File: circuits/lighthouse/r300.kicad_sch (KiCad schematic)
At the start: 18 parts, among them Q3 2N7002K, U1 R300, U6 AMS1117-3.3

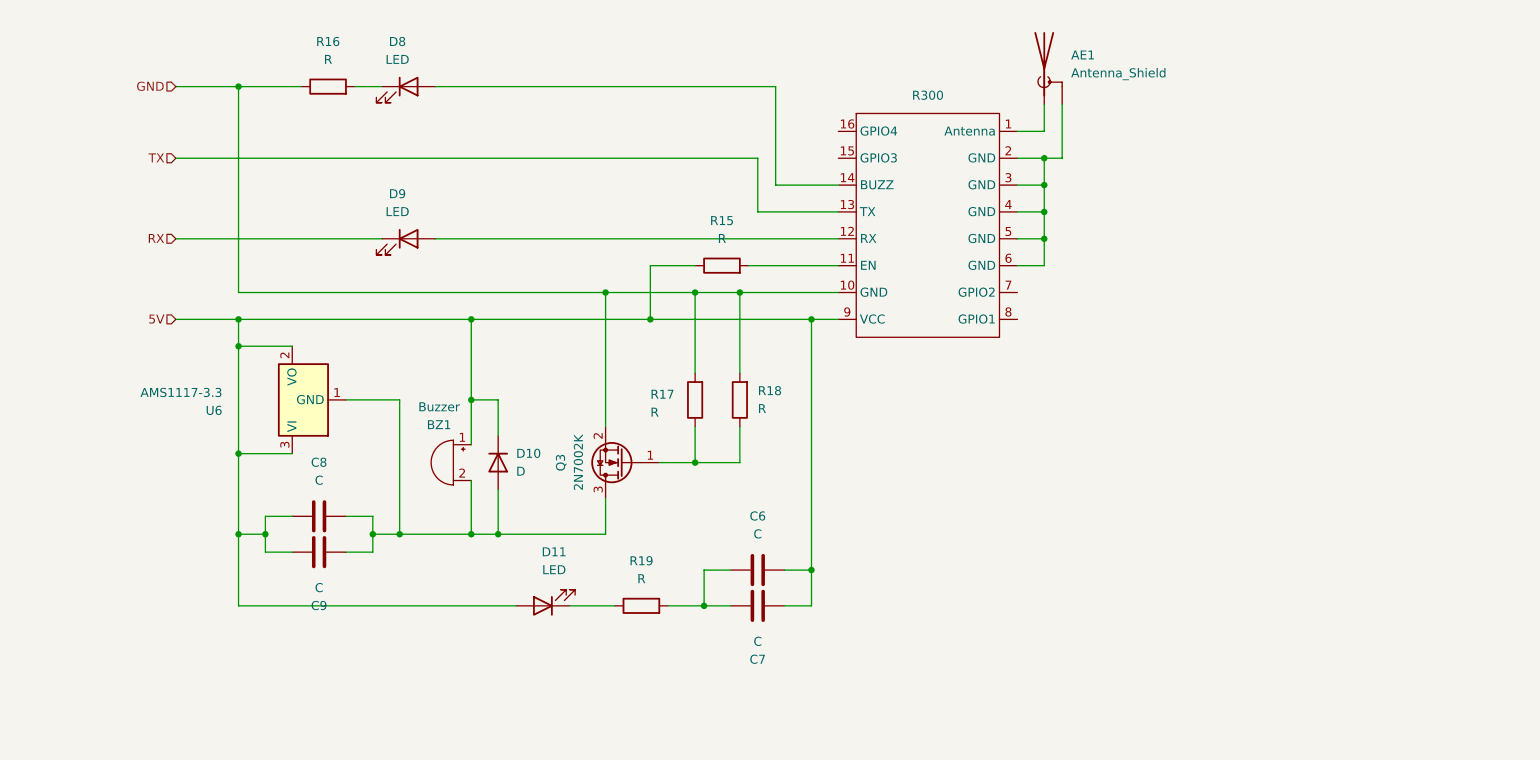
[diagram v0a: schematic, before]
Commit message: The circuit now has all the values in place
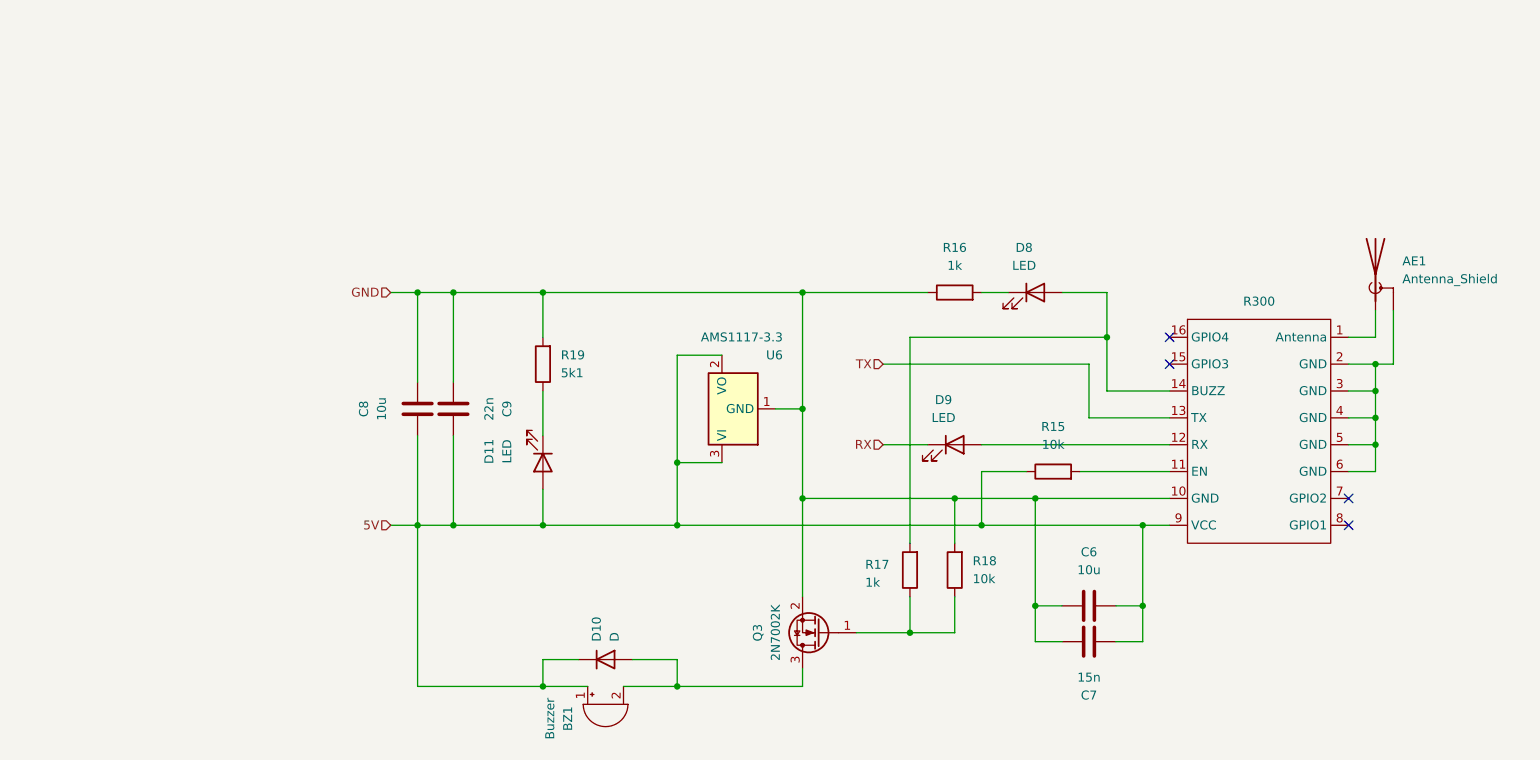
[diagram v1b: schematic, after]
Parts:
- C6, C8: value C -> 10u
- C7: value C -> 15n
- C9: value C -> 22n
- R15, R18: value R -> 10k
- R16, R17: value R -> 1k
- R19: value R -> 5k1
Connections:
- net GND: now also C6.1, C7.1, C8.2, C9.2, R19.2, U6.1 (GND); no longer R17.2
- net at D8.2 (A), U1.14 (BUZZ): now also R17.2
- net at BZ1.2 (-), D10.2 (A), Q3.3 (D): no longer C8.2, C9.2, U6.1 (GND)
- no-connect marks 0 -> 4
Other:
- moved on the sheet: AE1, BZ1, C6, C7, C8, C9, D10, D11, D8, D9, Q3, R15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

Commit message: Rewamped the pcb
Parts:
- BZ1: footprint Buzzer_Beeper:Buzzer_12x9.5RM7.6 -> Buzzer_Beeper:MagneticBuzzer_PUI_AT-0927-TT-6-R
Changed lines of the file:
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@@
 			)
 		)
-		(property "Footprint" "Buzzer_Beeper:Buzzer_12x9.5RM7.6"
+		(property "Footprint" "Buzzer_Beeper:MagneticBuzzer_PUI_AT-0927-TT-6-R"
 			(at 97.79 123.825 90)
 			(effects

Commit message: Cleaned up schematics
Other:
- moved on the sheet: AE1, BZ1, C6, C7, C8, C9, D10, D11, D8, D9, Q3, R15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

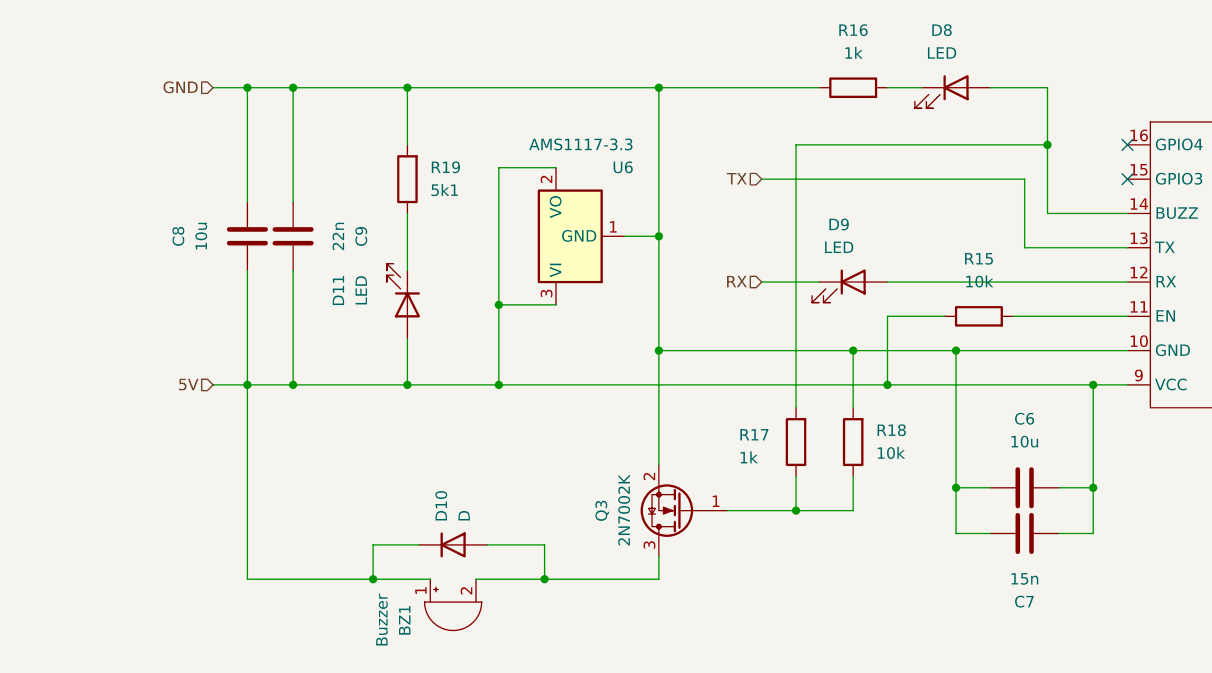
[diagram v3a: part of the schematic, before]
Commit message: Added bulk capacitors, fuses and battery power sense
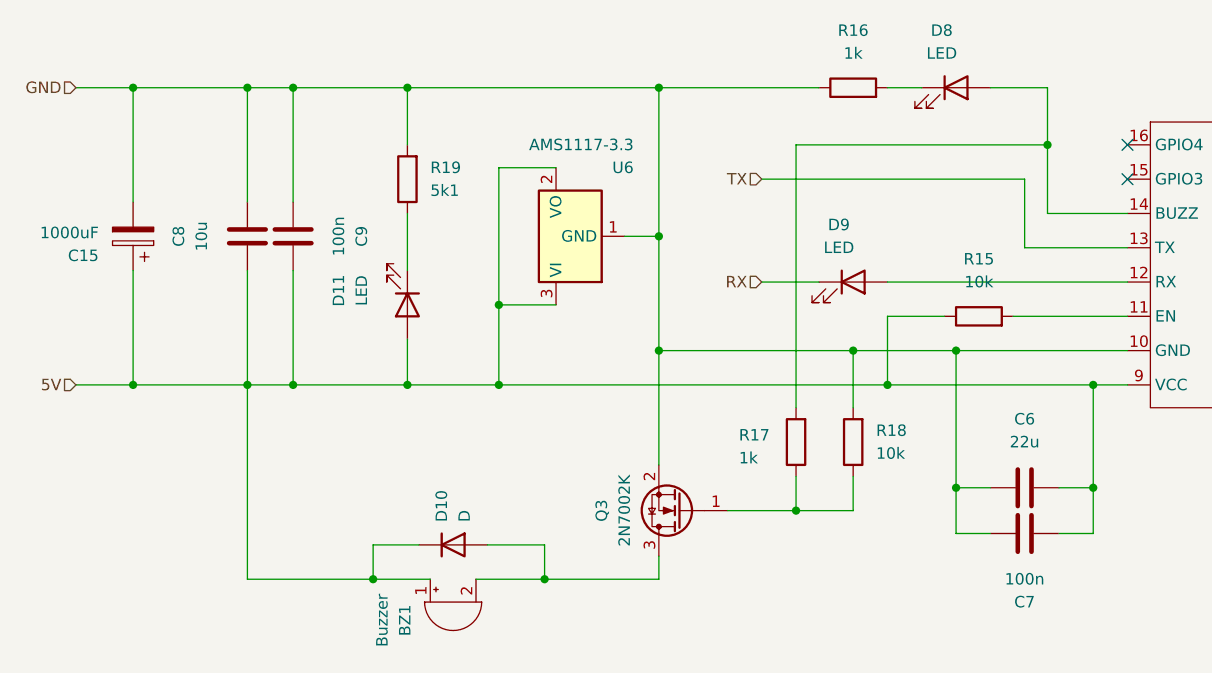
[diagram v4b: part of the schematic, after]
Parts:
- added C15: 1000uF, Capacitor_THT:CP_Radial_D10.0mm_P5.00mm, symbol Device:C_Polarized
- C6: value 10u -> 22u
- C7: value 15n -> 100n
- C9: value 22n -> 100n
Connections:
- net 5V: now also C15.1
- net GND: now also C15.2
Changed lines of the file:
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@@
+	)
+	(junction
+		(at 29.21 34.29)
+		(diameter 0)
+		(color 0 0 0 0)
 	)
 	(junction
@@
 		(color 0 0 0 0)
 	)
+	(junction
+		(at 29.21 67.31)
+		(diameter 0)
+		(color 0 0 0 0)
+	)
 	(no_connect
 		(at 139.7 44.45)
@@
 	(wire
 		(pts
+			(xy 29.21 34.29) (xy 41.91 34.29)
+		)
+		(stroke
+			(width 0)
+			(type default)
+		)
+	)
+	(wire
+		(pts
 			(xy 127 59.69) (xy 139.7 59.69)
 		)
@@
 	(wire
 		(pts
+			(xy 29.21 34.29) (xy 29.21 46.99)
+		)
+		(stroke
+			(width 0)
+			(type default)
+		)
+	)
+	(wire
+		(pts
 			(xy 87.63 34.29) (xy 87.63 50.8)
 		)
@@
 	(wire
 		(pts
-			(xy 38.1 67.31) (xy 41.91 67.31)
+			(xy 22.86 67.31) (xy 29.21 67.31)
 		)
 		(stroke
@@
 	(wire
 		(pts
-			(xy 38.1 34.29) (xy 41.91 34.29)
+			(xy 22.86 34.29) (xy 29.21 34.29)
 		)
 		(stroke
@@
 	(wire
 		(pts
+			(xy 29.21 54.61) (xy 29.21 67.31)
+		)
+		(stroke
+			(width 0)
+			(type default)
+		)
+	)
+	(wire
+		(pts
 			(xy 135.89 78.74) (xy 135.89 83.82)
 		)
@@
 		(pts
 			(xy 109.22 81.28) (xy 109.22 77.47)
+		)
+		(stroke
+			(width 0)
+			(type default)
+		)
+	)
+	(wire
+		(pts
+			(xy 29.21 67.31) (xy 41.91 67.31)
 		)
 		(stroke
@@
 	(hierarchical_label "5V"
 		(shape input)
-		(at 38.1 67.31 180)
+		(at 22.86 67.31 180)
 		(effects
 			(font
@@
 	(hierarchical_label "GND"
 		(shape input)
-		(at 38.1 34.29 180)
+		(at 22.86 34.29 180)
 		(effects
 			(font
@@
 			)
 		)
-		(property "Value" "10u"
+		(property "Value" "22u"
 			(at 128.27 73.66 90)
 			(effects
@@
 				(path "/7210d03b-7565-45ff-aaca-ad566f37cd67/b8f7ab96-114b-4177-9af0-0e115f506aa3"
 					(reference "C6")
+					(unit 1)
+				)
+			)
+		)
+	)
+	(symbol
+		(lib_id "Device:C_Polarized")
+		(at 29.21 50.8 180)
+		(unit 1)
+		(exclude_from_sim no)
+		(in_bom yes)
+		(on_board yes)
+		(dnp no)
+		(property "Reference" "C15"
+			(at 25.4 52.9591 0)
+			(effects
+				(font
+					(size 1.27 1.27)
+				)
+				(justify left)
+			)
+		)
+		(property "Value" "1000uF"
+			(at 25.4 50.4191 0)
+			(effects
+				(font
+					(size 1.27 1.27)
+				)
+				(justify left)
+			)
+		)
+		(property "Footprint" "Capacitor_THT:CP_Radial_D10.0mm_P5.00mm"
+			(at 28.2448 46.99 0)
+			(effects
+				(font
+					(size 1.27 1.27)
+				)
+				(hide yes)
+			)
+		)
+		(property "Datasheet" "~"
+			(at 29.21 50.8 0)
+			(effects
+				(font
+					(size 1.27 1.27)
+				)
+				(hide yes)
+			)
+		)
+		(property "Description" "Polarized capacitor"
+			(at 29.21 50.8 0)
+			(effects
+				(font
+					(size 1.27 1.27)
+				)
+				(hide yes)
+			)
+		)
+		(pin "1"
+		)
+		(pin "2"
+		)
+		(instances
+			(project ""
+				(path "/7210d03b-7565-45ff-aaca-ad566f37cd67/b8f7ab96-114b-4177-9af0-0e115f506aa3"
+					(reference "C15")
 					(unit 1)
 				)
@@
 			)
 		)
-		(property "Value" "22n"
+		(property "Value" "100n"
 			(at 52.07 50.8 90)
 			(effects
@@
 			)
 		)
-		(property "Value" "15n"
+		(property "Value" "100n"
 			(at 128.27 88.9 90)
 			(effects

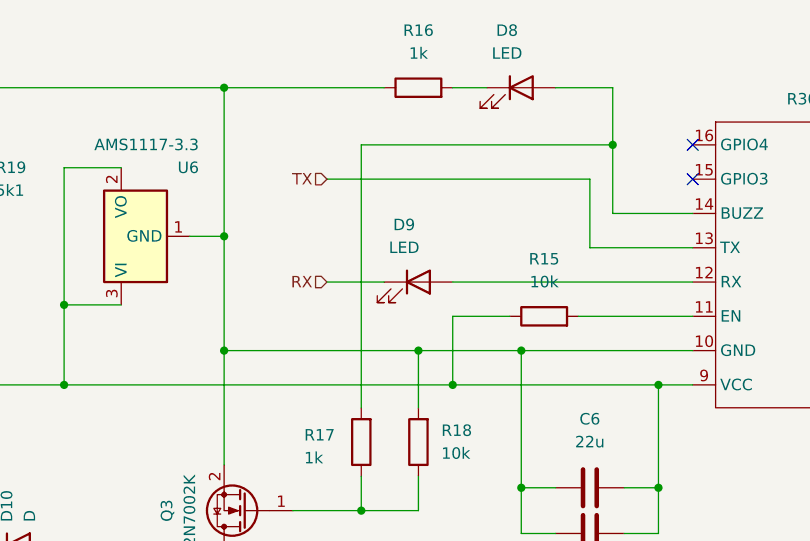
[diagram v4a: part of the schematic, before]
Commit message: Finalized the board (experiment pending)
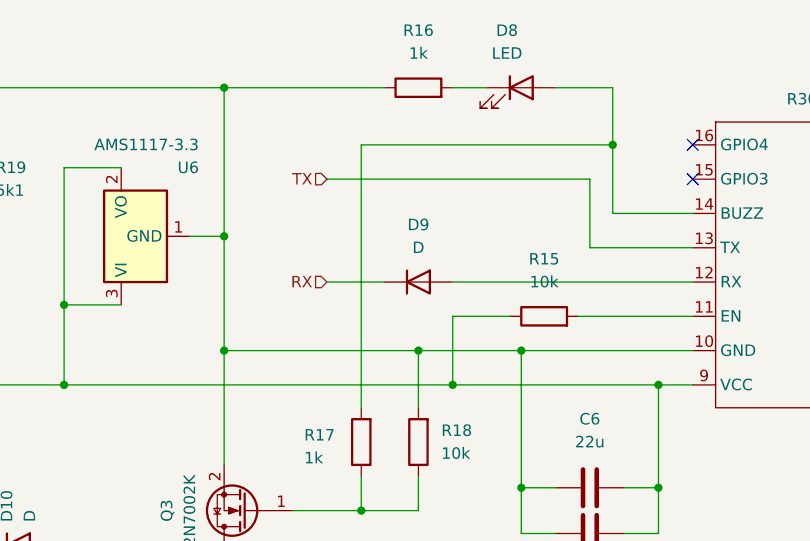
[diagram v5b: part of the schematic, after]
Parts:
- removed D9: LED, LED_SMD:LED_1206_3216Metric_Pad1.42x1.75mm_HandSolder, symbol Device:LED
- added D9: D, LED_SMD:LED_1206_3216Metric_Pad1.42x1.75mm_HandSolder, symbol Device:D
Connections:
- net RX: now also D9.1 (K)
- net at U1.12 (RX): now also D9.2 (A)
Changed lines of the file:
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@@
-	)
-	(symbol
-		(lib_id "Device:LED")
-		(at 109.22 55.88 0)
-		(unit 1)
-		(exclude_from_sim no)
-		(in_bom yes)
-		(on_board yes)
-		(dnp no)
-		(property "Reference" "D9"
-			(at 107.6325 49.53 0)
-			(effects
-				(font
-					(size 1.27 1.27)
-				)
-			)
-		)
-		(property "Value" "LED"
-			(at 107.6325 52.07 0)
-			(effects
-				(font
-					(size 1.27 1.27)
-				)
-			)
-		)
-		(property "Footprint" "LED_SMD:LED_1206_3216Metric_Pad1.42x1.75mm_HandSolder"
-			(at 109.22 55.88 0)
-			(effects
-				(font
-					(size 1.27 1.27)
-				)
-				(hide yes)
-			)
-		)
-		(property "Datasheet" "~"
-			(at 109.22 55.88 0)
-			(effects
-				(font
-					(size 1.27 1.27)
-				)
-				(hide yes)
-			)
-		)
-		(property "Description" "Light emitting diode"
-			(at 109.22 55.88 0)
-			(effects
-				(font
-					(size 1.27 1.27)
-				)
-				(hide yes)
-			)
-		)
-		(property "Sim.Pins" "1=K 2=A"
-			(at 109.22 55.88 0)
-			(effects
-				(font
-					(size 1.27 1.27)
-				)
-				(hide yes)
-			)
-		)
-		(pin "2"
-		)
-		(pin "1"
-		)
-		(instances
-			(project ""
-				(path "/7210d03b-7565-45ff-aaca-ad566f37cd67/b8f7ab96-114b-4177-9af0-0e115f506aa3"
-					(reference "D9")
-					(unit 1)
-				)
-			)
-		)
 	)
 	(symbol
@@
 					(unit 1)
 				)
+			)
+		)
+	)
+	(symbol
+		(lib_id "Device:D")
+		(at 109.22 55.88 0)
+		(unit 1)
+		(exclude_from_sim no)
+		(in_bom yes)
+		(on_board yes)
+		(dnp no)
+		(fields_autoplaced yes)
+		(property "Reference" "D9"
+			(at 109.22 49.53 0)
+			(effects
+				(font
+					(size 1.27 1.27)
+				)
+			)
+		)
+		(property "Value" "D"
+			(at 109.22 52.07 0)
+			(effects
+				(font
+					(size 1.27 1.27)
+				)
+			)
+		)
+		(property "Footprint" "LED_SMD:LED_1206_3216Metric_Pad1.42x1.75mm_HandSolder"
+			(at 109.22 55.88 0)
+			(effects
+				(font
+					(size 1.27 1.27)
+				)
+				(hide yes)
+			)
+		)
+		(property "Datasheet" "~"
+			(at 109.22 55.88 0)
+			(effects
+				(font
+					(size 1.27 1.27)
+				)
+				(hide yes)
+			)
+		)
+		(property "Description" "Diode"
+			(at 109.22 55.88 0)
+			(effects
+				(font
+					(size 1.27 1.27)
+				)
+				(hide yes)
+			)
+		)
+		(property "Sim.Device" "D"
+			(at 109.22 55.88 0)
+			(effects
+				(font
+					(size 1.27 1.27)
+				)
+				(hide yes)
+			)
+		)
+		(property "Sim.Pins" "1=K 2=A"
+			(at 109.22 55.88 0)
+			(effects
+				(font
+					(size 1.27 1.27)
+				)
+				(hide yes)
+			)
+		)
+		(pin "2"
+		)
+		(pin "1"
+		)
+		(instances
+			(project ""
+				(path "/7210d03b-7565-45ff-aaca-ad566f37cd67/b8f7ab96-114b-4177-9af0-0e115f506aa3"
+					(reference "D9")
+					(unit 1)
+				)

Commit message: Production ready board
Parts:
- removed D10, D9: D, LED_SMD:LED_1206_3216Metric_Pad1.42x1.75mm_HandSolder, symbol Device:D
- removed U6: AMS1117-3.3, Package_TO_SOT_SMD:SOT-223-3_TabPin2, symbol Regulator_Linear:AMS1117-3.3
- added D10: SS24A, Diode_SMD:D_SMA, symbol Device:D_Schottky
- BZ1: footprint Buzzer_Beeper:MagneticBuzzer_PUI_AT-0927-TT-6-R -> Buzzer_Beeper:Buzzer_12x9.5RM7.6
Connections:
- net 5V: now also D10.1 (K)
- net RX: now also U1.12 (RX)
- net at BZ1.2 (-), Q3.3 (D): now also D10.2 (A)
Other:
- moved on the sheet: BZ1, C15, C8, C9, D11, R19

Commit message: Schematic title block
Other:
- company: (none) -> Brno University of Technology
- title: (none) -> UHF RFID reader
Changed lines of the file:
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@@
 	(generator_version "9.0")
 	(paper "A5")
+	(title_block
+		(title "UHF RFID reader")
+		(date "2026-03-25")
+		(rev "1")
+		(company "Brno University of Technology")
+		(comment 1 "Embedded Implementation of an Attendance System for Integration")
+		(comment 2 "into an Enterprise Application")
+		(comment 3 "Author: Jakub Hloušek")
+		(comment 4 "Supervisor: Ing. Michal Bastl, Ph.D")
+	)
 	(junction
 		(at 59.69 34.29)
